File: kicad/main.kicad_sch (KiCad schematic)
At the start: 37 parts, among them J1 Barrel_Jack, SW1 Reset, SW2 SW_DIP_x08, U1 KM1810VM88, U10 L7805, U11 15 MHz, U12 8255, U2 W27C512, U3 AS6C4008-55PCN, U4 74HC573, U5 74HC573, U6 74HC273, U6 ATF16V8, U7 DS1813-5+, U8 74HC00, U8 74HC244

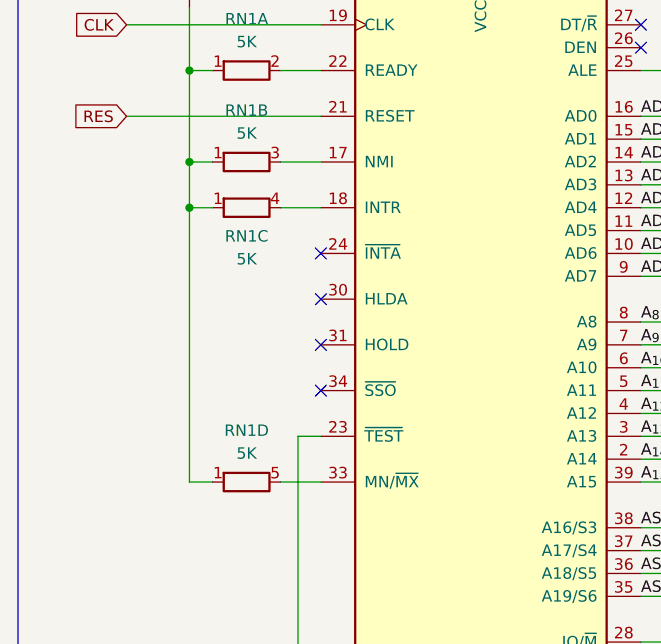
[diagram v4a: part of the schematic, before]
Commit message: Fix HOLD, INT & address decoder equations
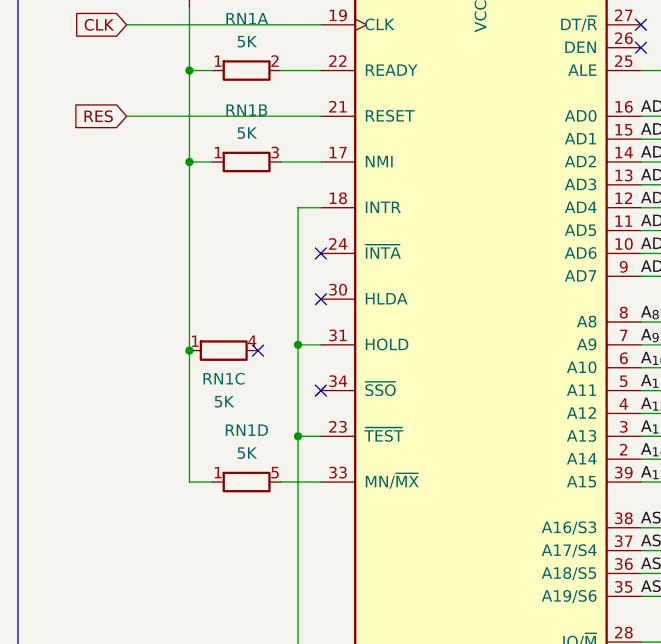
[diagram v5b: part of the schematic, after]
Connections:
- net GND: now also U1.18 (INTR), U1.31 (HOLD)
- net at RN1.4 (R3.2): no longer U1.18 (INTR)
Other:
- moved on the sheet: RN1C
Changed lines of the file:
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@@
   (junction (at 139.065 116.84) (diameter 0) (color 0 0 0 0)
   )
-  (junction (at 35.56 60.325) (diameter 0) (color 0 0 0 0)
-  )
   (junction (at 48.895 165.1) (diameter 0) (color 0 0 0 0)
   )
@@
   (junction (at 335.28 234.95) (diameter 0) (color 0 0 0 0)
   )
+  (junction (at 47.625 85.725) (diameter 0) (color 0 0 0 0)
+  )
   (junction (at 199.39 240.03) (diameter 0) (color 0 0 0 0)
   )
@@
   )
   (junction (at 199.39 245.11) (diameter 0) (color 0 0 0 0)
+  )
+  (junction (at 35.56 76.2) (diameter 0) (color 0 0 0 0)
+  )
+  (junction (at 47.625 75.565) (diameter 0) (color 0 0 0 0)
   )
   (junction (at 199.39 237.49) (diameter 0) (color 0 0 0 0)
@@
   (no_connect (at 374.65 156.845))
   (no_connect (at 50.165 65.405))
-  (no_connect (at 50.165 75.565))
   (no_connect (at 85.725 42.545))
   (no_connect (at 167.005 106.68))
@@
   (no_connect (at 177.165 250.825))
   (no_connect (at 374.65 154.305))
+  (no_connect (at 43.18 76.2))
   (no_connect (at 167.005 109.22))
   (bus_entry (at 137.16 52.07) (size -2.54 -2.54)
@@
     (stroke (width 0) (type default))
   )
+  (wire (pts (xy 35.56 76.2) (xy 35.56 90.805))
+    (stroke (width 0) (type default))
+  )
   (bus (pts (xy 211.455 63.5) (xy 211.455 60.96))
     (stroke (width 0) (type default))
@@
     (stroke (width 0) (type default))
   )
-  (wire (pts (xy 35.56 60.325) (xy 35.56 90.805))
+  (wire (pts (xy 35.56 55.245) (xy 35.56 76.2))
     (stroke (width 0) (type default))
   )
@@
     (stroke (width 0) (type default))
   )
-  (wire (pts (xy 45.72 60.325) (xy 50.165 60.325))
+  (wire (pts (xy 47.625 60.325) (xy 50.165 60.325))
     (stroke (width 0) (type default))
   )
@@
     (stroke (width 0) (type default))
   )
-  (wire (pts (xy 35.56 55.245) (xy 35.56 60.325))
-    (stroke (width 0) (type default))
-  )
   (bus (pts (xy 132.715 230.505) (xy 132.715 227.965))
     (stroke (width 0) (type default))
   )
+  (wire (pts (xy 47.625 75.565) (xy 47.625 85.725))
+    (stroke (width 0) (type default))
+  )
   (wire (pts (xy 213.995 66.04) (xy 218.44 66.04))
     (stroke (width 0) (type default))
@@
     (stroke (width 0) (type default))
   )
+  (wire (pts (xy 47.625 60.325) (xy 47.625 75.565))
+    (stroke (width 0) (type default))
+  )
   (bus (pts (xy 309.88 51.435) (xy 309.88 53.975))
     (stroke (width 0) (type default))
@@
     (stroke (width 0) (type default))
   )
-  (wire (pts (xy 38.1 60.325) (xy 35.56 60.325))
-    (stroke (width 0) (type default))
-  )
   (bus (pts (xy 211.455 38.1) (xy 211.455 35.56))
     (stroke (width 0) (type default))
   )
   (wire (pts (xy 100.33 158.75) (xy 102.87 158.75))
+    (stroke (width 0) (type default))
+  )
+  (wire (pts (xy 50.165 75.565) (xy 47.625 75.565))
     (stroke (width 0) (type default))
   )
@@
     )
   )
-  (symbol (lib_id "Device:R_Network04_Split") (at 41.91 60.325 90) (unit 3)
+  (symbol (lib_id "Device:R_Network04_Split") (at 39.37 76.2 90) (unit 3)
     (in_bom yes) (on_board yes) (dnp no) (fields_autoplaced)
-    (property "Reference" "RN1" (at 41.91 63.5 90)
+    (property "Reference" "RN1" (at 39.37 79.375 90)
       (effects (font (size 1.27 1.27)))
     )
-    (property "Value" "5K" (at 41.91 66.04 90)
+    (property "Value" "5K" (at 39.37 81.915 90)
       (effects (font (size 1.27 1.27)))
     )
-    (property "Footprint" "Resistor_THT:R_Array_SIP5" (at 41.91 62.357 90)
+    (property "Footprint" "Resistor_THT:R_Array_SIP5" (at 39.37 78.232 90)
       (effects (font (size 1.27 1.27)) hide)
     )
-    (property "Datasheet" "http://www.vishay.com/docs/31509/csc.pdf" (at 41.91 60.325 0)
+    (property "Datasheet" "http://www.vishay.com/docs/31509/csc.pdf" (at 39.37 76.2 0)
       (effects (font (size 1.27 1.27)) hide)
     )
